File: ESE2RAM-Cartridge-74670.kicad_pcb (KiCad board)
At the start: 2 copper layers, 100 x 60.5 mm, 27 parts, among them IC1 4M SRAM, IC2 4M SRAM, J1 BUS_MSX, J2 8M, U1 74HC670, U2 74HC670, U3 74HC138, U4 74HC00, U5 74HC32

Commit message: Updated Schematic & Gerber data.
Updated to revision 4.
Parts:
- C8: moved to B.Cu
- C9: value 47u -> 10u
- J1: footprint ProjectLibrary:BUS_MSX_SHORT_CARD -> ProjectLibrary:BUS_MSX_CARD_SHORT
- moved D2 4.29 mm to (41.6, 123.0)
- moved R4 2.54 mm to (61.4, 123.8)
- moved C8 2.50 mm to (69.5, 150.4), turned to 180 degrees
- moved BT1 0.50 mm to (51.4, 117.1)
- moved D1 0.50 mm to (41.6, 111.1)
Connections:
- C8 pad 1: +5V -> GND
- C8 pad 2: GND -> +5V
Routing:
- net +5V: track 234.8 -> 246.9 mm
- net Net-(BT1-+): track 13.8 -> 9.73 mm
- net Net-(D2-K): track 19.8 -> 23.8 mm
- net /D0: track 85.7 -> 82.7 mm
- net /EN_WR: track 70.6 -> 73.1 mm
- net GND: track 227.4 -> 228.2 mm
- net /~{RAM0_CE}: track 38.6 -> 37.9 mm
- net Net-(J1-SW1): track 11.0 -> 10.5 mm
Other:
- board text added: "似非²RAM rev.4 Goripon Hardware"
- board text removed: "似非²RAM rev.3 Goripon Hardware"

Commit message: Updated Schematic & Gerber data
回路図データとガーバーデータを更新
Updated Schematic & Gerber data.
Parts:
- C9: value 10u -> 47u
- moved IC2 40.5 mm to (118.8, 89.1)
- moved J1 40.5 mm to (102.3, 119.3)
- moved BT1 40.5 mm to (58.7, 77.3)
- moved C4 40.5 mm to (84.5, 76.3)
- moved C5 40.5 mm to (97.3, 76.4)
- moved C7 40.5 mm to (99.8, 84.0)
- moved C9 40.5 mm to (65.2, 106.6)
- moved D1 40.5 mm to (48.9, 71.3)
- moved IC1 40.5 mm to (126.4, 68.7)
- moved J2 40.5 mm to (97.5, 61.1)
- moved R2 40.5 mm to (125.2, 84.0)
- moved R3 40.5 mm to (71.7, 72.8)
- moved R4 40.5 mm to (68.7, 84.0)
- moved RN1 40.5 mm to (94.7, 91.6)
- moved S1 40.5 mm to (74.9, 67.2)
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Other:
- outline, holes or cut-outs redrawn

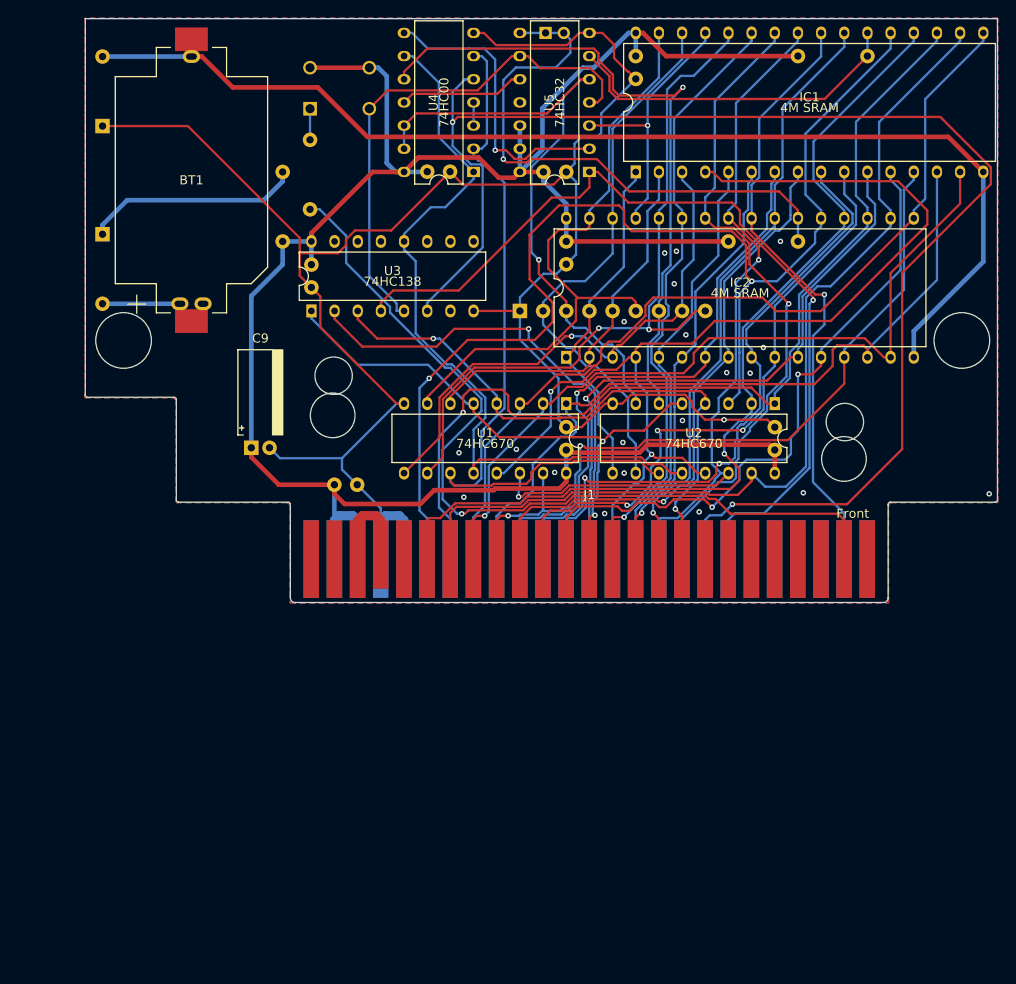
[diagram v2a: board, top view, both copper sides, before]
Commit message: PCB modified
PCBを修正
PCB modified.
U4, U5, IC1の位置を下にずらした
U4, U5, and IC1 shifted downward.
その他細かな修正
Other minor modifications.
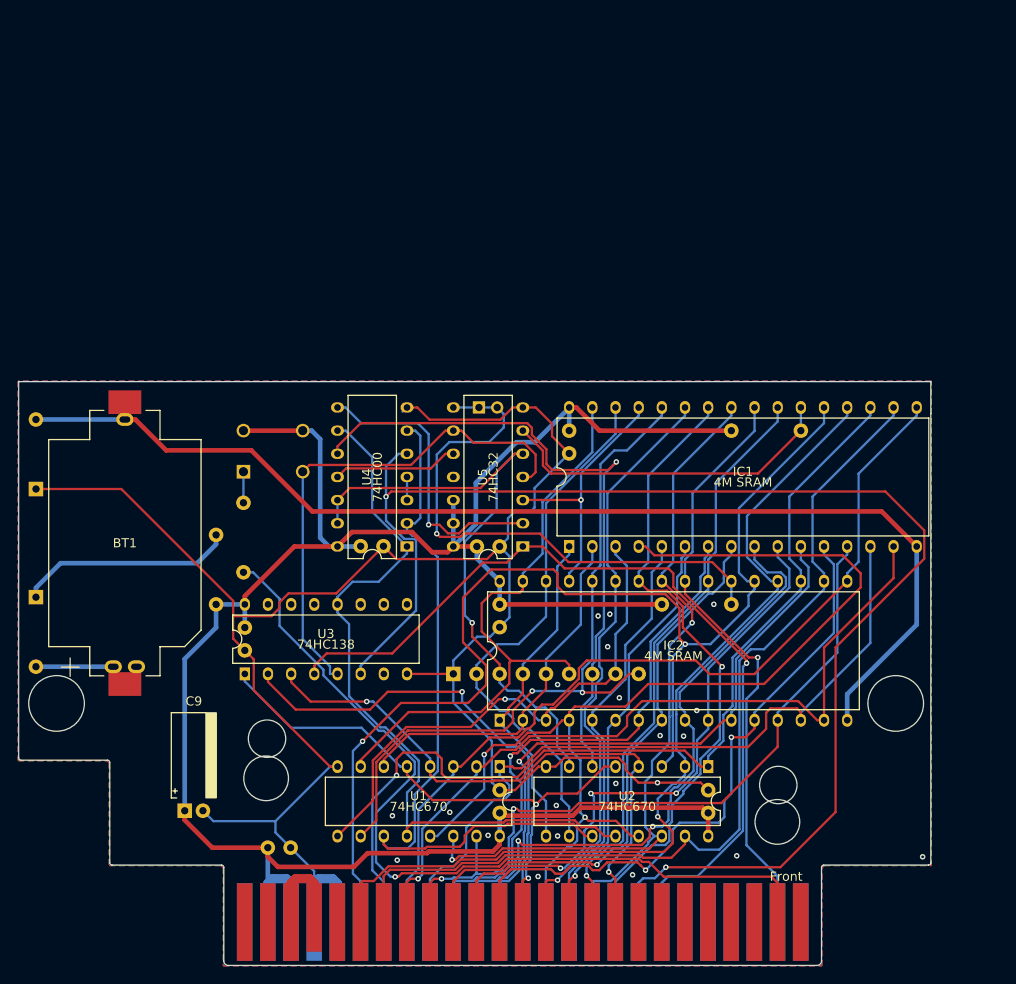
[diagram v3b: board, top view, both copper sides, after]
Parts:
- moved C4 41.7 mm to (77.2, 117.4)
- moved C5 41.7 mm to (90.0, 117.4)
- moved C6 41.7 mm to (100.1, 104.7)
- moved R1 41.7 mm to (125.5, 104.7)
- moved IC1 41.7 mm to (119.1, 109.8)
- moved J2 41.7 mm to (90.2, 102.2)
- moved U4 41.7 mm to (78.5, 109.8)
- moved U5 41.7 mm to (91.2, 109.8)
- moved IC2 40.5 mm to (111.5, 128.9)
- moved J1 40.5 mm to (95.0, 159.1)
- moved BT1 40.5 mm to (51.4, 117.1)
- moved C7 40.5 mm to (92.5, 123.8)
- moved C9 40.5 mm to (57.9, 146.4)
- moved D1 40.5 mm to (41.6, 111.1)
- moved R2 40.5 mm to (117.9, 123.8)
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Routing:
- net /~{WR}: track 96.2 -> 94.2 mm
- net GND: track 228.2 -> 226.4 mm
- net /~{RESET}: track 157.0 -> 155.2 mm
- net /~{RAM_WE}: track 29.9 -> 28.6 mm
- net /RAM_A18: track 38.3 -> 37.0 mm
- net /D3: track 96.9 -> 95.6 mm
- net /A0: track 71.7 -> 70.4 mm
- net Net-(U1-~{Er}): track 82.1 -> 80.8 mm
- net /D4: track 104.6 -> 103.3 mm
- net /D2: track 86.8 -> 85.6 mm
- net /D1: track 83.8 -> 82.6 mm
- net /RAM_A14: track 59.1 -> 57.8 mm
- net /A4: track 64.6 -> 63.3 mm
- net /RAM_A16: track 41.8 -> 40.5 mm
- net /D0: track 82.7 -> 81.4 mm
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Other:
- outline, holes or cut-outs redrawn
- board text added: "WR"
- board text added: "似非²RAM rev.5 Goripon Hardware"
- board text removed: "似非²RAM rev.4 Goripon Hardware"

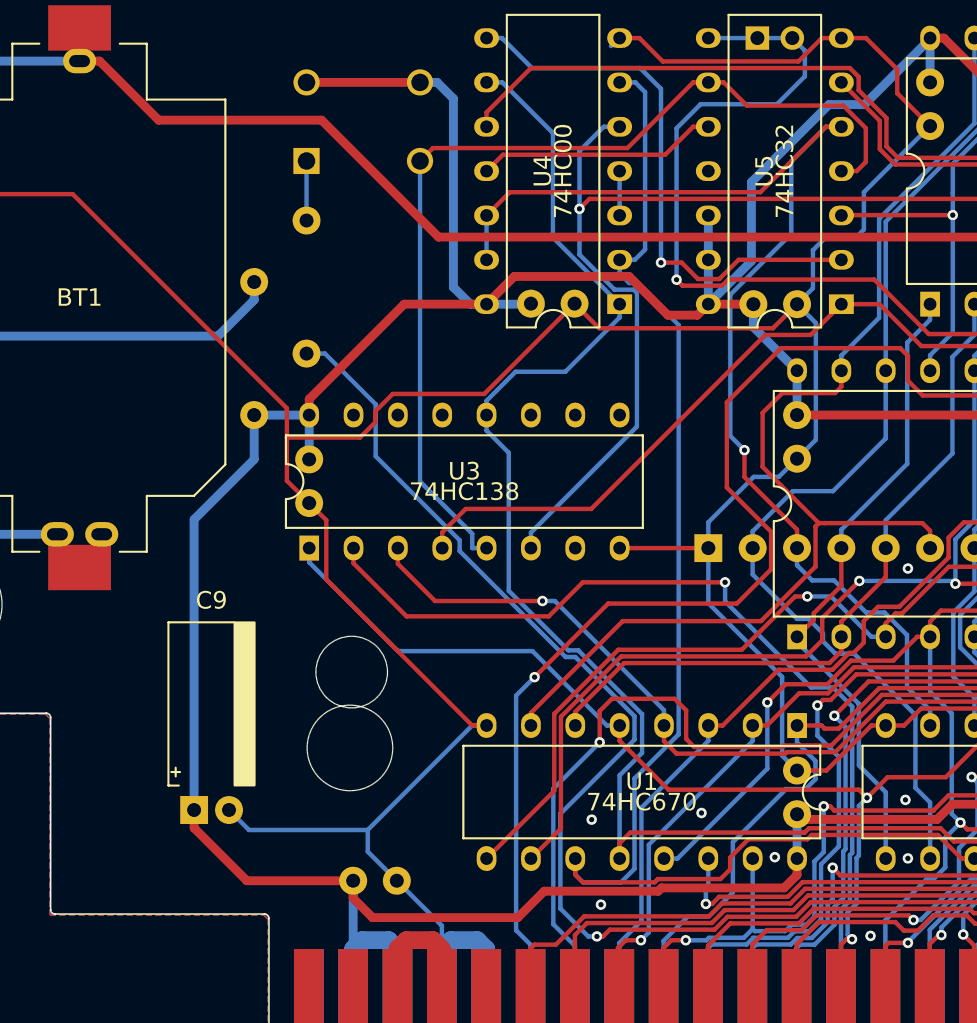
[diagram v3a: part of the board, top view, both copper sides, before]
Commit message: Modified Schematic
一部MSX機種での動作不良修正のため74HC00/74HC32/74HC138を74AHCシリーズに変更
Changed 74HC00/74HC32/74HC138 to 74AHC series to fix malfunction on some MSX models.
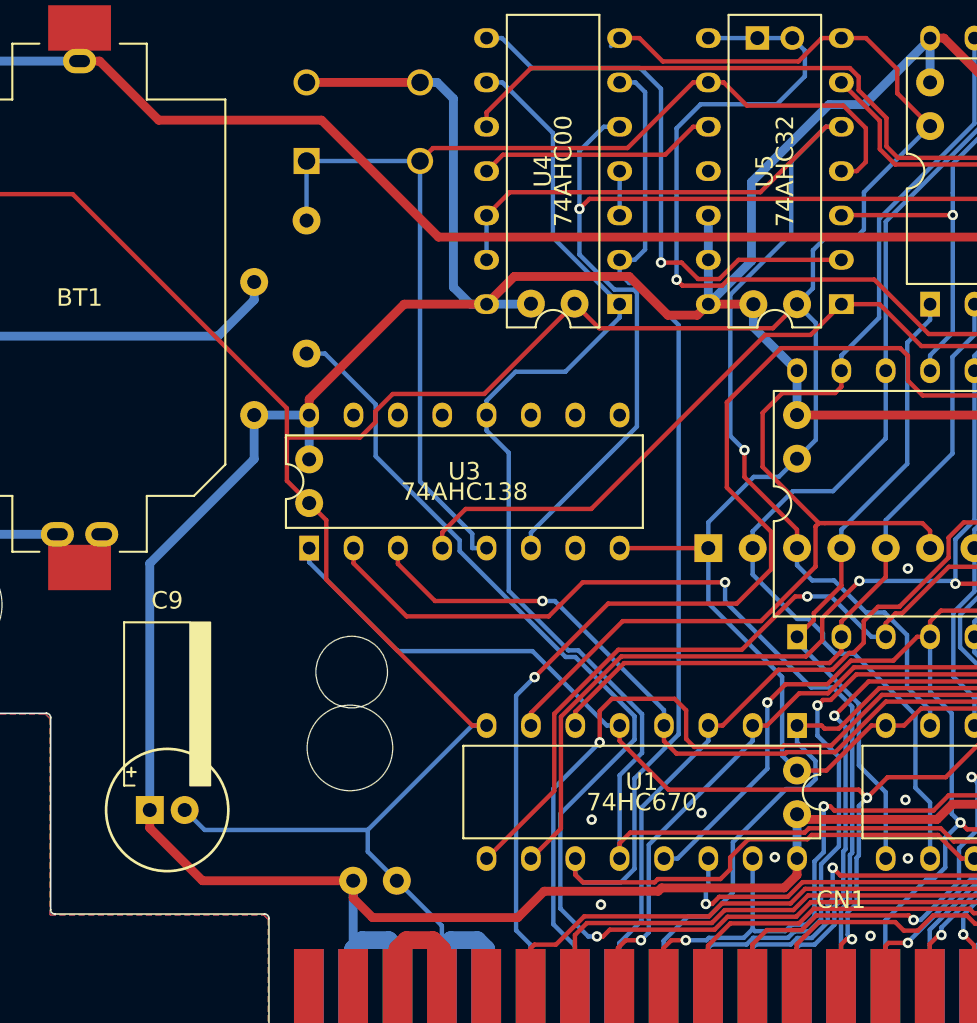
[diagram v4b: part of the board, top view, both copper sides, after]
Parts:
- removed J2: 8M, Connector_PinHeader_2.00mm:PinHeader_1x02_P2.00mm_Vertical
- added CN1: BUS_MSX, ProjectLibrary:BUS_MSX_CARD_SHORT, F.Cu at (95.0, 159.1)
- J1: value BUS_MSX -> 8M; footprint ProjectLibrary:BUS_MSX_CARD_SHORT -> Connector_PinHeader_2.00mm:PinHeader_1x02_P2.00mm_Vertical; moved to B.Cu
- U3: value 74HC138 -> 74AHC138
- U4: value 74HC00 -> 74AHC00
- U5: value 74HC32 -> 74AHC32
- moved J1 57.1 mm to (90.2, 102.2), turned to -90 degrees
- moved C9 2.54 mm to (55.4, 146.4)
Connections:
- J1 pad 1: unconnected-(J1-~{CS1}-Pad1) -> /~{RAM1_CE}
- J1 pad 2: unconnected-(J1-~{CS2}-Pad2) -> /~{RAM1_CE}
- R3 pad 1: Net-(S1-COM_1) -> /~{SLOTSELECT}
- S1 pad 1: Net-(S1-COM_1) -> /~{SLOTSELECT}
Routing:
- net Net-(J1-SW1): track 10.5 -> 0.00 mm
- net Net-(CN1-SW1): track 0.00 -> 10.5 mm
- net /~{SLOTSELECT}: track 56.3 -> 66.2 mm
- net +5V: track 246.4 -> 250.0 mm
- net Net-(S1-COM_1): track 3.41 -> 0.00 mm
- net GND: track 226.4 -> 228.9 mm

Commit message: Modified PCB
基板上のシルク印刷のバージョン番号を修正
Corrected version number on PCB silkscreen.
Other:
- board text added: "似非²RAM rev.6 Goripon Hardware"
- board text removed: "似非²RAM rev.5 Goripon Hardware"
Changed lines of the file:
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@@
   (gr_line (start 139.73 99.36) (end 39.73 99.36)
     (stroke (width 0.1) (type default)) (layer "Edge.Cuts"))
-  (gr_text "似非²RAM rev.5\nGoripon Hardware" (at 119.13 111.81) (layer "B.SilkS")
+  (gr_text "似非²RAM rev.6\nGoripon Hardware" (at 119.13 111.81) (layer "B.SilkS")
     (effects (font (size 1.53 1.53) (thickness 0.153)) (justify mirror))
   )

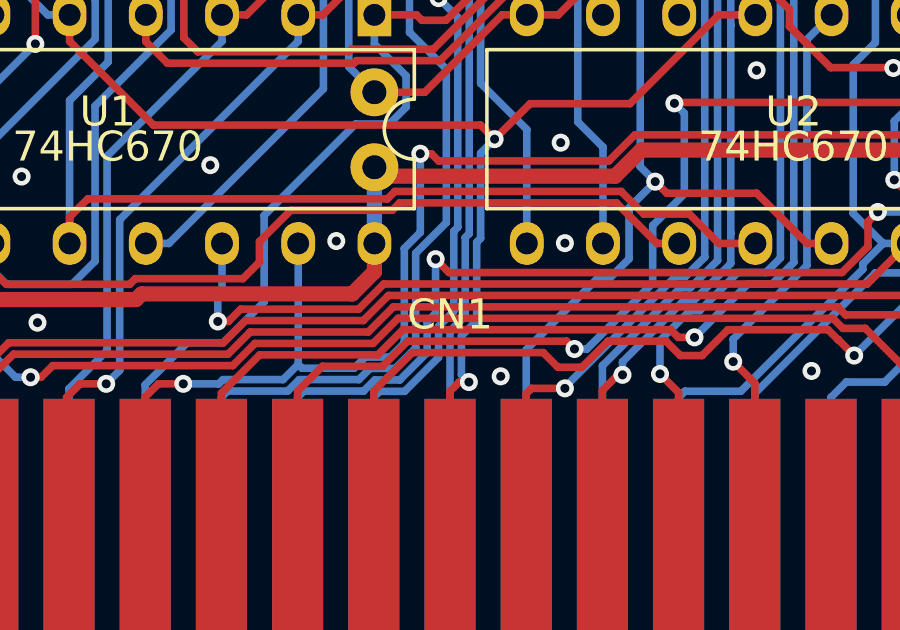
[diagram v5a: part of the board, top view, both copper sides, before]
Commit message: Modified ESE2BOOT.COM & Schematic
ESE2BOOT.COMのバグ修正
Fixed a bug in ESE2BOOT.COM
回路図データの微修正
Minor corrections to schematic data.
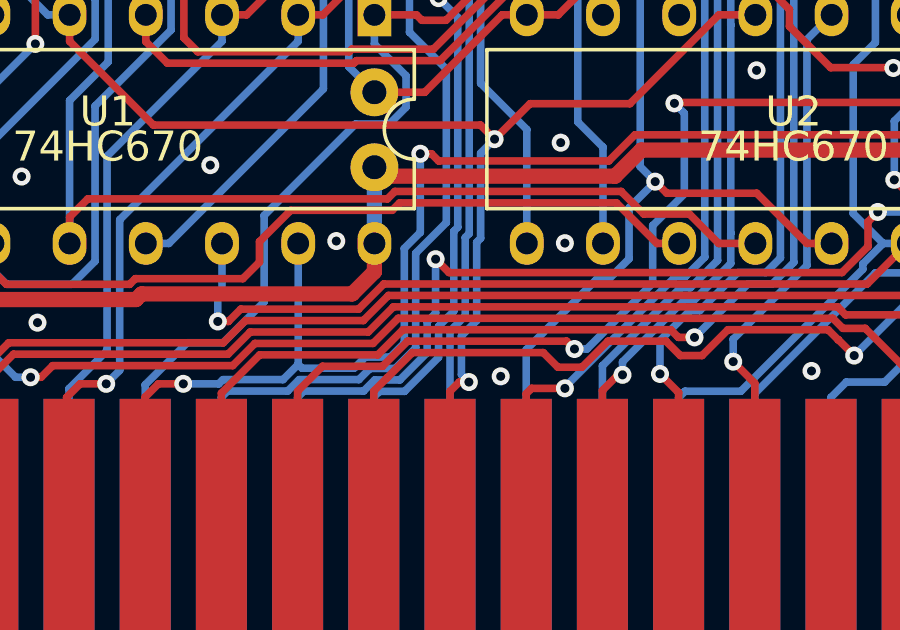
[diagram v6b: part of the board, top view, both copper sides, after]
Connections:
- net -BATT renamed /BATT-
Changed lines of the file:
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@@
   (title_block
     (title "ESE2RAM Cartridge (74x670 version)")
-    (date "2025-04-06")
+    (date "2025-04-11")
     (rev "6")
     (company "Goripon Hardware")
@@
   (net 1 "+5V")
   (net 2 "GND")
-  (net 3 "-BATT")
+  (net 3 "/BATT-")
   (net 4 "/RAM_A18")
   (net 5 "/RAM_A16")
@@
         (effects (font (size 1 1) (thickness 0.153)) (justify top))
     )
-    (fp_text user "${REFERENCE}" (at 0 0) (layer "F.Fab")
-        (effects (font (size 1 1) (thickness 0.15)))
+    (fp_text user "${REFERENCE}" (at 0 0 180) (layer "F.Fab")
+        (effects (font (size 1 1) (thickness 0.153)))
     )
     (fp_line (start -2.65 -8.95) (end -2.65 8.95)
@@
       (net 18 "/D2") (pinfunction "DQ2") (pintype "passive"))
     (pad "16" thru_hole oval (at -7.62 19.05 90) (size 1.43 1.13) (drill 0.73) (layers "*.Cu" "*.Mask")
-      (net 3 "-BATT") (pinfunction "VSS") (pintype "passive"))
+      (net 3 "/BATT-") (pinfunction "VSS") (pintype "passive"))
     (pad "17" thru_hole oval (at 7.62 19.05 90) (size 1.43 1.13) (drill 0.73) (layers "*.Cu" "*.Mask")
       (net 19 "/D3") (pinfunction "DQ3") (pintype "passive"))
@@
       (net 75 "Net-(BT1-+)") (pinfunction "+") (pintype "passive"))
     (pad "2" smd rect (at -15.45 0 90) (size 2.6 3.6) (layers "F.Cu" "F.Paste" "F.Mask")
-      (net 3 "-BATT") (pinfunction "-") (pintype "passive"))
+      (net 3 "/BATT-") (pinfunction "-") (pintype "passive"))
     (pad "2" thru_hole oval (at -13.55 0 90) (size 1.4 1.9) (drill oval 0.7 1.2) (layers "*.Cu" "*.Mask")
-      (net 3 "-BATT") (pinfunction "-") (pintype "passive"))
+      (net 3 "/BATT-") (pinfunction "-") (pintype "passive"))
     (model "${KICAD6_3DMODEL_DIR}/Battery.3dshapes/BatteryHolder_Keystone_1060_1x2032.wrl"
       (offset (xyz 0 0 0))
@@
       (net 18 "/D2") (pinfunction "DQ2") (pintype "passive"))
     (pad "16" thru_hole oval (at -7.62 19.05 90) (size 1.43 1.13) (drill 0.73) (layers "*.Cu" "*.Mask")
-      (net 3 "-BATT") (pinfunction "VSS") (pintype "passive"))
+      (net 3 "/BATT-") (pinfunction "VSS") (pintype "passive"))
     (pad "17" thru_hole oval (at 7.62 19.05 90) (size 1.43 1.13) (drill 0.73) (layers "*.Cu" "*.Mask")
       (net 19 "/D3") (pinfunction "DQ3") (pintype "passive"))
@@
     (property "ki_description" "MSX cartridge bus connector")
     (attr through_hole exclude_from_pos_files exclude_from_bom)
-    (fp_text reference "CN1" (at 0 -7.5) (layer "F.SilkS")
+    (fp_text reference "CN1" (at 0 -7.5) (layer "F.SilkS") hide
         (effects (font (size 1 1) (thickness 0.15)))
     )
@@
         (effects (font (size 1 1) (thickness 0.153)) (justify left bottom))
     )
-    (fp_text user "Tall cartridge size" (at 0 -123.037 unlocked) (layer "Dwgs.User")
-        (effects (font (size 1 1) (thickness 0.15)) (justify top))
-    )
     (fp_text user "Short cartridge size" (at 0 -59.037 unlocked) (layer "Dwgs.User")
         (effects (font (size 1 1) (thickness 0.153)) (justify top))
     )
     (fp_text user "PCB 10cm square size" (at 0 -95.537 unlocked) (layer "Dwgs.User")
+        (effects (font (size 1 1) (thickness 0.15)) (justify top))
+    )
+    (fp_text user "Tall cartridge size" (at 0 -123.037 unlocked) (layer "Dwgs.User")
         (effects (font (size 1 1) (thickness 0.15)) (justify top))
     )
@@
       (net 2 "GND") (pinfunction "K") (pintype "passive"))
     (pad "2" thru_hole oval (at 7.62 0 90) (size 1.6 1.6) (drill 0.8) (layers "*.Cu" "*.Mask")
-      (net 3 "-BATT") (pinfunction "A") (pintype "passive"))
+      (net 3 "/BATT-") (pinfunction "A") (pintype "passive"))
     (model "${KICAD6_3DMODEL_DIR}/Diode_THT.3dshapes/D_DO-35_SOD27_P7.62mm_Horizontal.wrl"
       (offset (xyz 0 0 0))
